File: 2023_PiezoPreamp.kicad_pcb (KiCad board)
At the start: 4 copper layers, 71 x 36.8 mm, 88 parts, among them J101 6.3mm stereo, J102 6.3mm stereo, J201 DC IN 5.5/2.1mm, J401 Spring Contact, U101 OPA145, U102 OPA145, U201 ZXMP3A17E6TA, U301 BC847BS,115

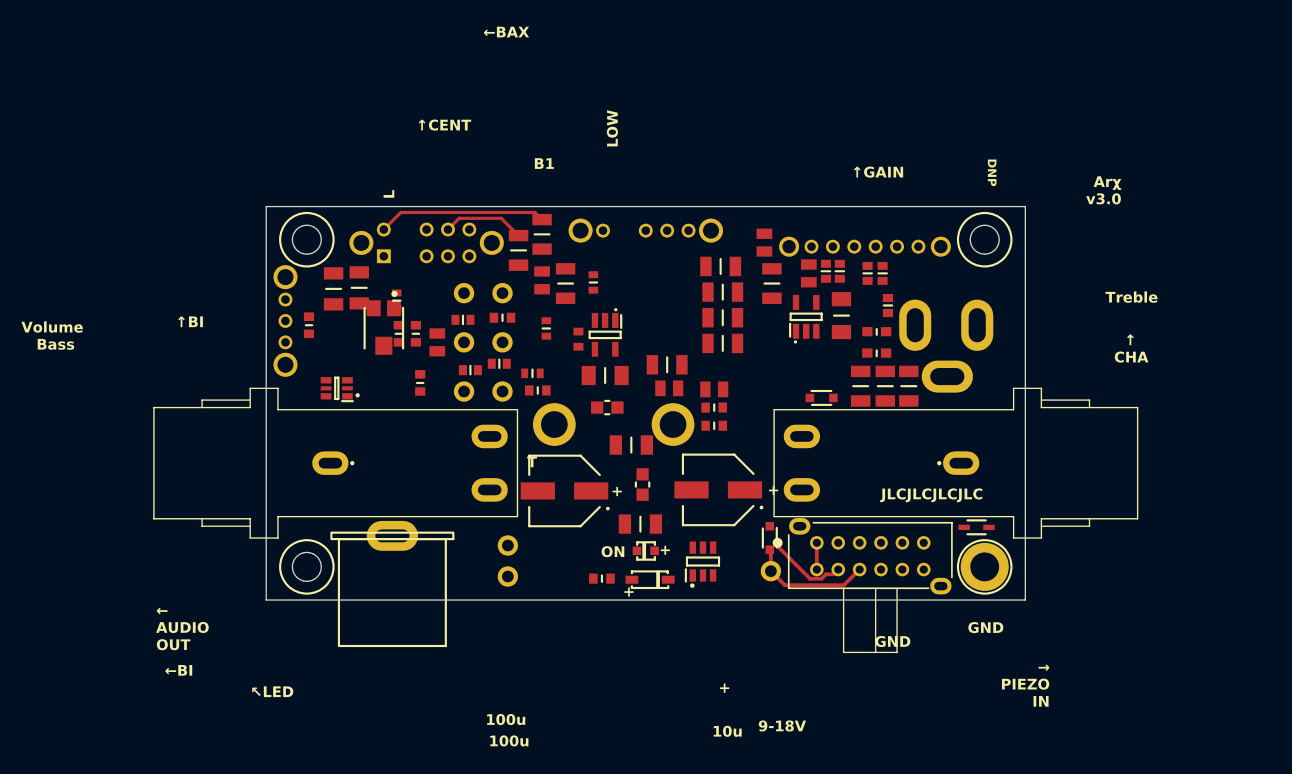
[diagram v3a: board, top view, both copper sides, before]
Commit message: fixing missing DC jack; continued working on the board layout
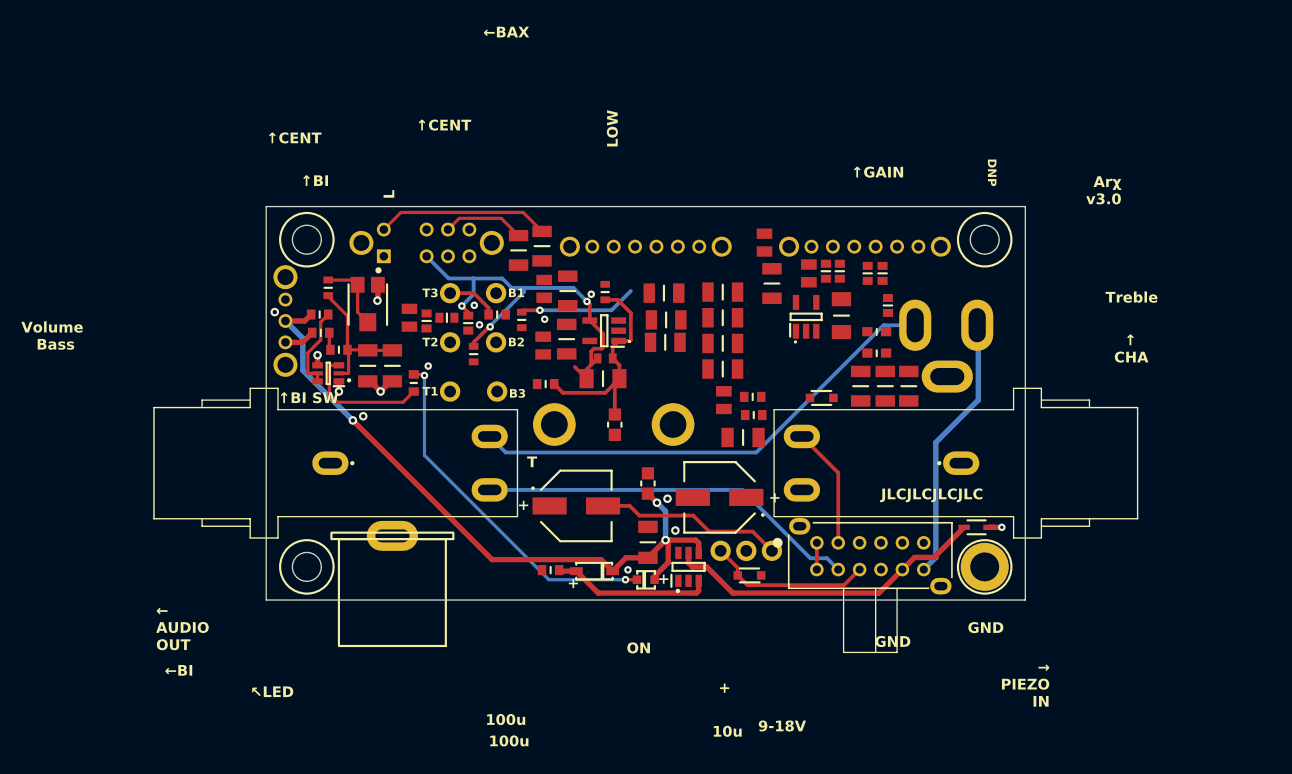
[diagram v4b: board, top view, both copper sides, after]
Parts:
- added Chp105: 220n, library:GRM31C5C1H224JE02L, F.Cu at (152.2, 87.8)
- added Chp107: 100n, library:GRM31C5C2A104JA01L, F.Cu at (152.3, 85.7)
- added Chp108: 68n, library:GRM31C5C1H683JA01L, F.Cu at (152.1, 83.2)
- R101, R102: footprint library:RT0603BRD07150RL_UL-M -> library:RT0603BRE07150RL_UL-M
- S102: value OS103011MA7QP1 -> SK14D01G6; footprint library:sw_OS103011MA7QP1 -> library:sw_SK14D01G6
- U201: value ZXMP3A17E6TA -> SOT95P285X140-6N
- moved H109 24.7 mm to (162.2, 107.2)
- moved H107 22.4 mm to (159.8, 107.2)
- moved C207 12.5 mm to (140.8, 88.0), turned to -90 degrees
- moved C202 10.5 mm to (159.5, 96.7), turned to 180 degrees
- moved C206 9.70 mm to (143.0, 87.5), turned to -90 degrees
- moved Chp106 9.60 mm to (157.6, 90.2), turned to 180 degrees
- moved R301 8.90 mm to (120.0, 86.8), turned to 0 degrees
- moved C302 7.93 mm to (126.7, 90.0), turned to 90 degrees
- moved C301 7.88 mm to (124.4, 90.0), turned to 90 degrees
- moved R303 6.51 mm to (120.7, 82.7), turned to 90 degrees
- moved R302 5.80 mm to (121.7, 88.5), turned to 0 degrees
- moved R103 5.79 mm to (134.3, 88.8), turned to 90 degrees
- moved Ct102 5.37 mm to (131.8, 85.5)
- moved D202 5.26 mm to (145.6, 109.2)
- moved H108 5.07 mm to (157.4, 107.2)
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- renumbered Chp105 to Chp106
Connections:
- net /1-ChargeAmpAndEQ/HPF_SW_10 renamed /1-ChargeAmpAndEQ/HPF_SW_1
- Chp106 pad 2: /1-ChargeAmpAndEQ/HPF_SW_3 -> /1-ChargeAmpAndEQ/HPF_SW_4
- S102 pad 3: /1-ChargeAmpAndEQ/HPF_SW_3 -> /1-ChargeAmpAndEQ/CH_A_OUT
- S102 pad 4: unconnected-(S102-3-Pad4) -> /1-ChargeAmpAndEQ/HPF_SW_4
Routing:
- net Vbi: track 0.00 -> 64.3 mm, vias 0 -> 3
- net DC_IN_NEG: track 0.00 -> 45.4 mm
- net /1-ChargeAmpAndEQ/BAX_A_INV: track 0.00 -> 39.7 mm, vias 0 -> 3
- net /3-BatteryIndicator/LED_K: track 0.00 -> 33.2 mm, vias 0 -> 2
- net /2-Power/DC_IN_ESD: track 0.00 -> 30.4 mm
- net AUDIO_OUT: track 7.21 -> 35.7 mm
- net /2-Power/DC_IN_POS: track 0.00 -> 25.0 mm
- net /1-ChargeAmpAndEQ/BAX_A_OUT: track 0.00 -> 21.2 mm
- net /1-ChargeAmpAndEQ/VOL_3: track 0.00 -> 17.5 mm
- net /2-Power/RP_GATE: track 0.00 -> 15.0 mm
- net /3-BatteryIndicator/BI_B1: track 0.00 -> 13.2 mm
- net /3-BatteryIndicator/BI_C2: track 0.00 -> 12.1 mm
- net PIEZO_IN: track 0.00 -> 11.4 mm
- net /1-ChargeAmpAndEQ/BAX_IN: track 0.00 -> 11.0 mm, vias 0 -> 1
- net /3-BatteryIndicator/BI_C1_B2: track 0.00 -> 7.91 mm
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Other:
- board text added: "B2"
- board text added: "B3"
- board text added: "T1"
- board text added: "T2"
- board text added: "T3"
- board text added: "↑BI SW"
